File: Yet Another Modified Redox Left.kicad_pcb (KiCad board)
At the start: 2 copper layers, 180 x 126 mm, 98 parts, among them J1 USB_B_Mini, J2 AudioJack4, K1 KEYSW, K10 KEYSW, K11 KEYSW, K12 KEYSW, K13 KEYSW, K14 KEYSW, K15 KEYSW, K16 KEYSW, K17 KEYSW, K18 KEYSW, K19 KEYSW, K2 KEYSW, K20 KEYSW, K21 KEYSW, K22 KEYSW, K23 KEYSW, K24 KEYSW, K25 KEYSW, K26 KEYSW, K27 KEYSW, K28 KEYSW, K29 KEYSW, K3 KEYSW, K30 KEYSW, K31 KEYSW, K32 KEYSW, K33 KEYSW, K34 KEYSW, K35 KEYSW, K4 KEYSW, K5 KEYSW, K6 KEYSW, K7 KEYSW, K8 KEYSW, K9 KEYSW, Q1 DMG2302U, Q2 DMG2302U, Q3 DMG2302U, U1 YAAJ_BluePill_Part_Like

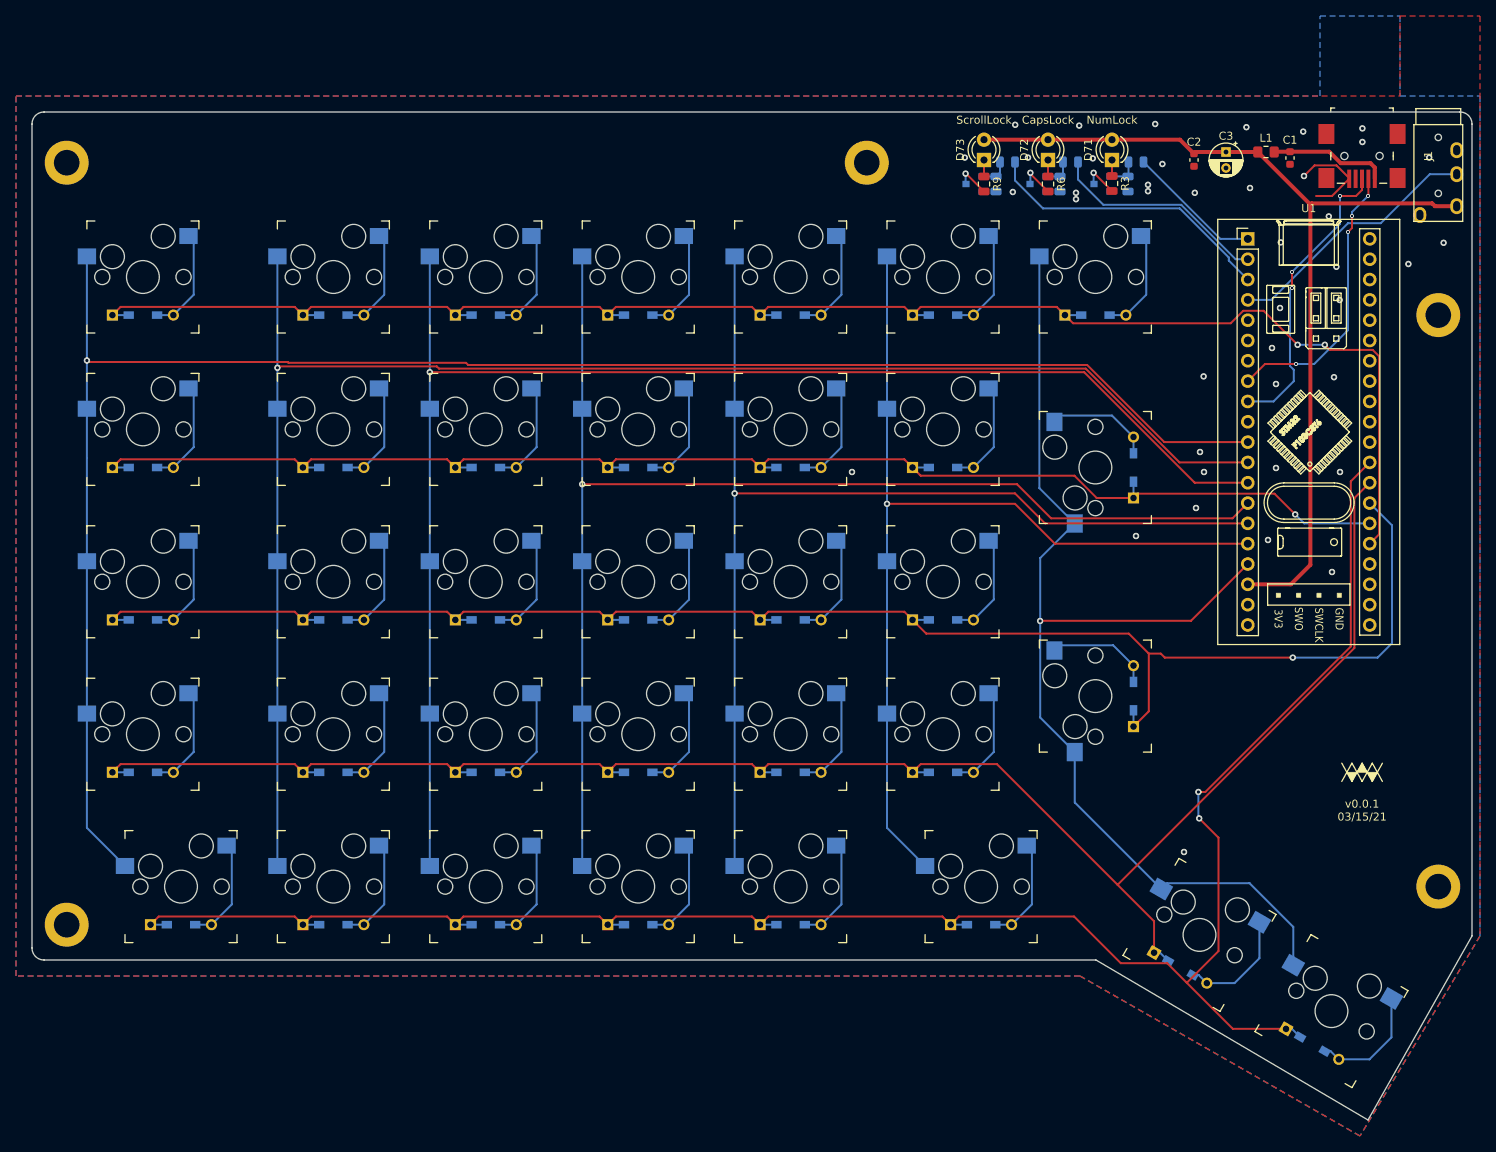
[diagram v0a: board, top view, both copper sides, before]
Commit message: Update to use rp2040 stamp
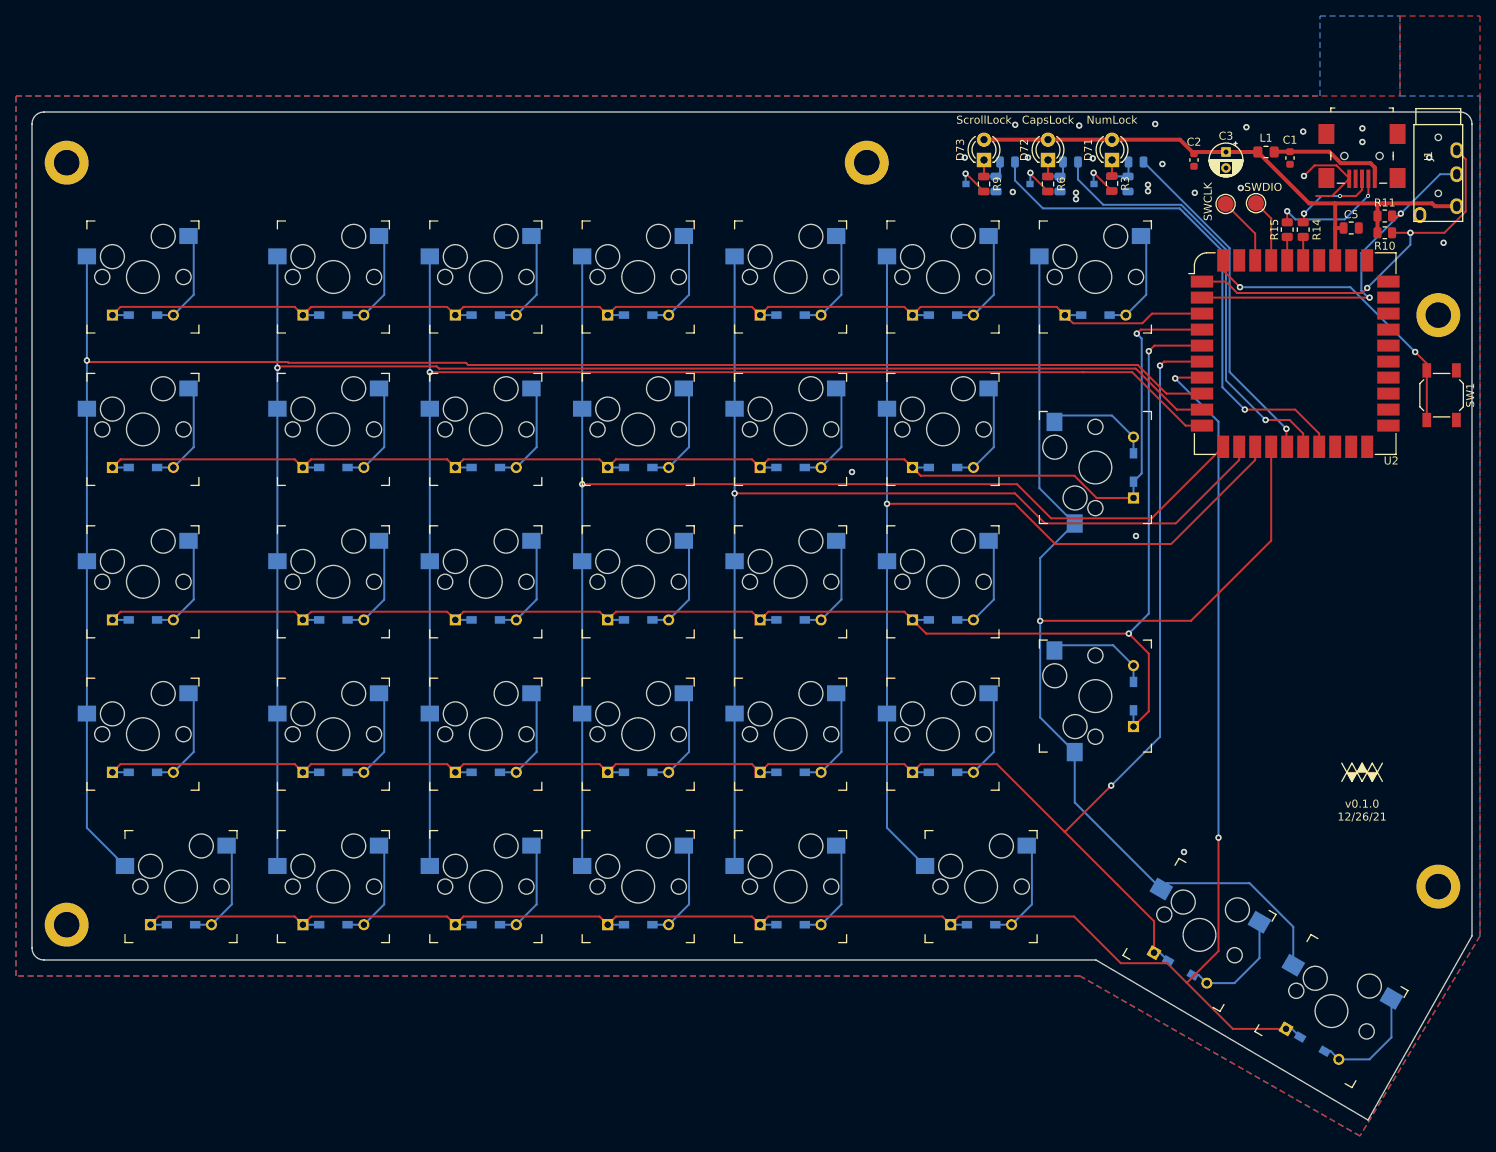
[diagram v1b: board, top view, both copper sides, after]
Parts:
- removed the REF** at (33.3, 128.6)
- removed the REF** at (204.8, 123.8)
- removed the REF** at (33.3, 33.3)
- removed the REF** at (133.3, 33.3)
- removed U1: YAAJ_BluePill_Part_Like, Footprints:YAAJ_BluePill_1
- added C5: 1uF, Capacitor_SMD:C_0805_2012Metric, F.Cu at (193.9, 41.5)
- added H6: MountingHole_3.2mm_M3_ISO14580_Pad, MountingHole:MountingHole_3.2mm_M3_ISO14580_Pad, F.Cu at (133.3, 33.3)
- added H7: MountingHole_3.2mm_M3_ISO14580_Pad, MountingHole:MountingHole_3.2mm_M3_ISO14580_Pad, F.Cu at (33.3, 33.3)
- added H8: MountingHole_3.2mm_M3_ISO14580_Pad, MountingHole:MountingHole_3.2mm_M3_ISO14580_Pad, F.Cu at (33.3, 128.6)
- added H9: MountingHole_3.2mm_M3_ISO14580_Pad, MountingHole:MountingHole_3.2mm_M3_ISO14580_Pad, F.Cu at (204.8, 123.8)
- added R10: 10kR, Resistor_SMD:R_0805_2012Metric, F.Cu at (198.1, 42.1)
- added R11: 10kR, Resistor_SMD:R_0805_2012Metric, F.Cu at (198.1, 40.0)
- added R14: 20R, Resistor_SMD:R_0805_2012Metric, F.Cu at (187.9, 41.7)
- added R15: 20R, Resistor_SMD:R_0805_2012Metric, F.Cu at (185.9, 41.7)
- added SW1: SW_Push, Button_Switch_SMD:SW_SPST_SKQG_WithoutStem, F.Cu at (205.2, 62.4)
- added SWCLK: TestPoint, TestPoint:TestPoint_Pad_D2.0mm, F.Cu at (178.2, 38.5)
- added SWDIO: TP, TestPoint:TestPoint_Pad_D2.0mm, F.Cu at (182.0, 38.4)
- added U2: RP2040_Stamp, RP2040_Stamp:RP2040_Stamp_SMD, F.Cu at (186.9, 57.2)
- renumbered REF** to H10
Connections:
- net Net-(C1-Pad1) renamed /VBUS
- J1 pad 4: (no net) -> Net-(J1-Pad4)
- J2 pad R1: /TX -> /SCL_M
- J2 pad R2: (no net) -> /SDA_M
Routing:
- net /SDA_M: track 0.00 -> 49.1 mm, vias 0 -> 2
- net /LR1: track 205.0 -> 156.5 mm, vias 2 -> 0
- net /SCL_M: track 0.00 -> 44.3 mm, vias 0 -> 2
- net /L+5V: track 116.7 -> 74.6 mm
- net Net-(SW1-Pad2): track 0.00 -> 38.6 mm, vias 0 -> 2
- net /TX: track 32.6 -> 0.00 mm
- net /SCROLL_LOCK: track 36.8 -> 65.1 mm, vias 0 -> 1
- net /CAPSLOCK: track 27.5 -> 54.7 mm, vias 0 -> 1
- net /D+: track 37.2 -> 11.0 mm, vias 3 -> 2
- net /NUM_LOCK: track 17.0 -> 43.0 mm, vias 0 -> 1
- net /D-: track 35.1 -> 15.3 mm, vias 4 -> 2
- net /LC7: track 141.7 -> 157.6 mm
- net Net-(TP2-Pad1): track 0.00 -> 8.58 mm
- net /LC2: track 202.5 -> 194.1 mm
- net /LC3: track 184.2 -> 175.7 mm
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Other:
- rule pad_to_mask_clearance: 0.05 -> 0
- board text added: "v0.1.0 12/26/21"
- board text removed: "v0.0.1 03/15/21"
